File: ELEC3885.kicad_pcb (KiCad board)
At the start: 4 copper layers, 190 x 145.2 mm, 159 parts, among them J1 MicInstIn, J2 LineIn, J3 HeadPhoneOut, J4 Conn_01x05_Female, J5 LineOutR, J6 LineOutL, J7 USB_B_Micro, J8 Conn_LiPo, SW1 SW_SPST, SW10 RotaryEncoder_Switch, SW11 RotaryEncoder_Switch, SW12 RotaryEncoder_Switch, SW13 RotaryEncoder_Switch, SW14 SW_Push, SW15 SW_Push, SW16 SW_Push, SW17 SW_Push, SW2 SW_Push, SW3 SW_Push, SW4 SW_Push, SW5 SW_Push, SW6 SW_Push, SW7 SW_Push, SW8 SW_Push, SW9 SW_Push, U1 NE5532, U10 74HC595, U11 LCD_Conn, U2 AP7313, U3 SGTL5000XNLA3, U4 Teensy4.1, U5 MCP73831-2-OT, U6 MT3608, U7 L7805, U8 74HC595, U9 74HC595

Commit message: Rev4 started, changing packages
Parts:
- D2: footprint LED_SMD:LED_0603_1608Metric -> LED_SMD:LED_0201_0603Metric
- U10, U8, U9: footprint Package_SO:SOP-16_4.4x10.4mm_P1.27mm -> Package_SO:SOP-16_3.9x9.9mm_P1.27mm
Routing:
- net +5V: track 424.7 -> 418.9 mm, vias 19 -> 20
- net Net-(U10-QH'): track 50.6 -> 56.2 mm, vias 2 -> 4
- net /Teensy/LED_RCLK: track 158.0 -> 153.7 mm, vias 8 -> 6
- net /Teensy/LED_SRCLK: track 149.9 -> 153.8 mm
- net Net-(U10-QA): track 7.63 -> 11.0 mm
- net Net-(U10-~{OE}): track 105.0 -> 108.3 mm
- net /Teensy/LED_DS: track 53.4 -> 55.8 mm
- net Net-(U9-QA): track 24.3 -> 25.9 mm
- net Net-(U8-QH): track 23.9 -> 25.0 mm
- net Net-(U8-SER): track 71.9 -> 71.4 mm

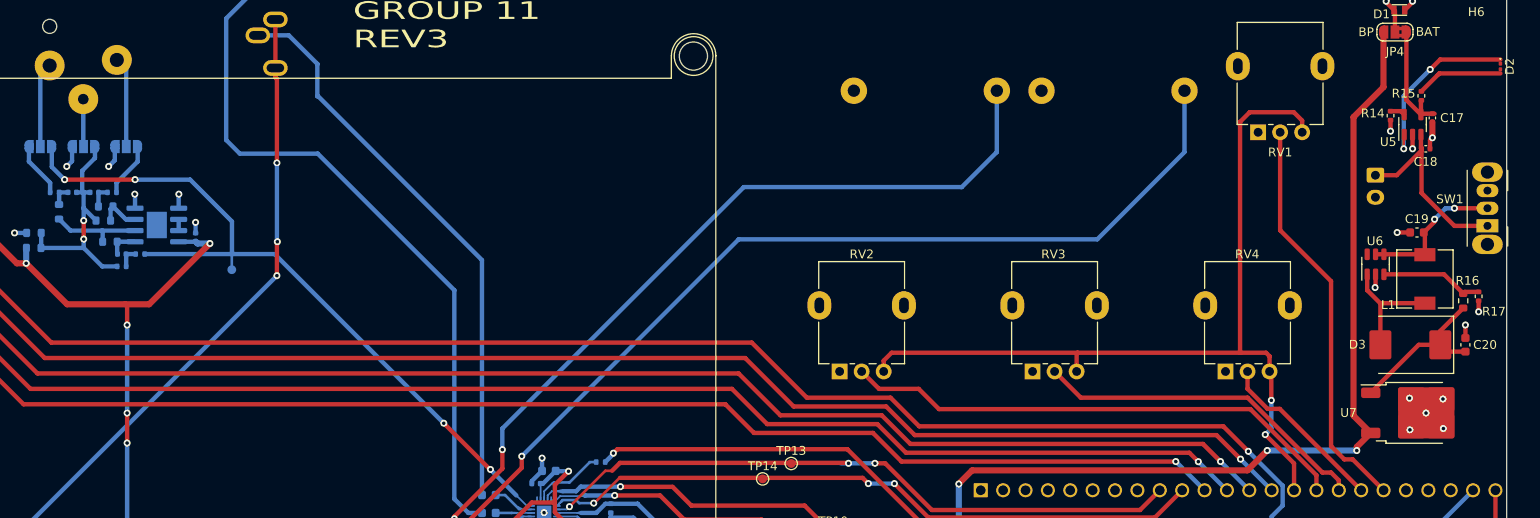
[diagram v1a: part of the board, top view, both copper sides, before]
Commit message: Footprints updated except codec
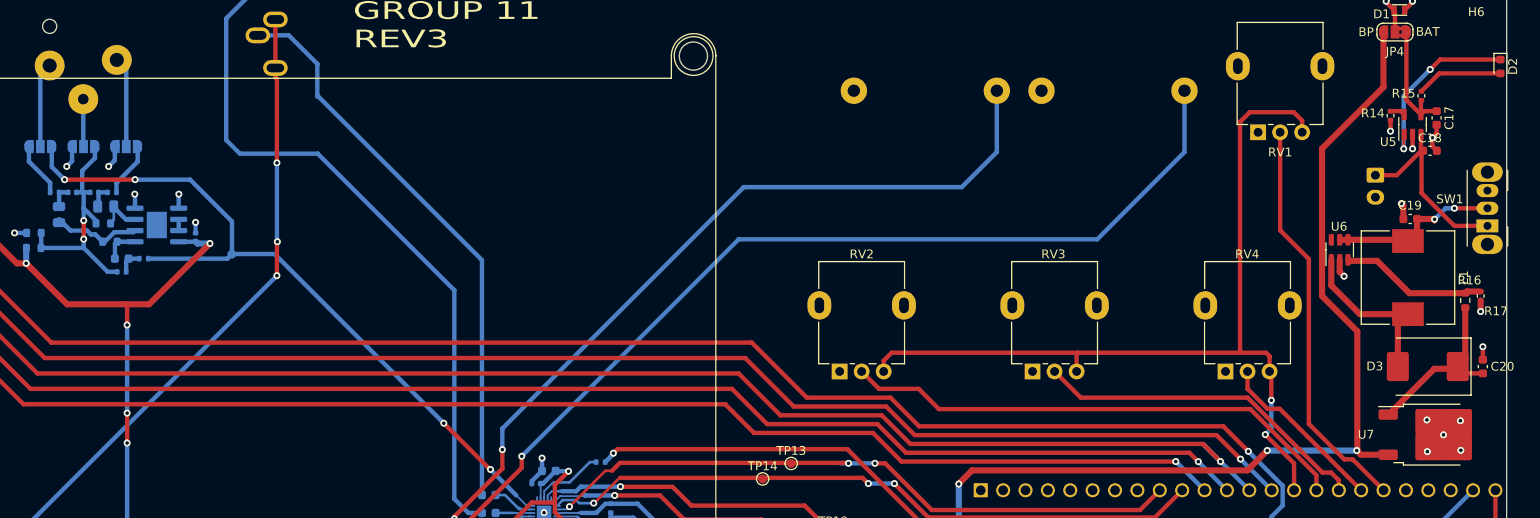
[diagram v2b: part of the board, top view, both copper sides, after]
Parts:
- C16, C17, C18: footprint Capacitor_SMD:C_0402_1005Metric -> Capacitor_SMD:C_0603_1608Metric
- D2: footprint LED_SMD:LED_0201_0603Metric -> LED_SMD:LED_0603_1608Metric
- L1: footprint Inductor_SMD:L_6.3x6.3_H3 -> Inductor_SMD:L_10.4x10.4_H4.8
- R8, R9: footprint Resistor_SMD:R_0603_1608Metric -> Resistor_SMD:R_0805_2012Metric
- moved U6 4.39 mm to (191.2, 51.5)
- moved C20 3.17 mm to (207.5, 64.8)
- moved D3 3.17 mm to (201.2, 64.8)
- moved U7 3.17 mm to (201.8, 72.5)
- moved L1 1.93 mm to (199.0, 54.6)
- moved TP7 1.75 mm to (65.5, 52.0)
- moved C19 1.71 mm to (199.2, 48.0)
- moved R13 0.66 mm to (55.5, 52.5)
- moved R12 0.62 mm to (53.0, 54.0)
- moved C18 0.53 mm to (201.5, 40.2)
- moved C16 0.52 mm to (53.0, 52.5)
- moved C17 0.48 mm to (202.2, 36.5)
- moved R10 0.32 mm to (50.9, 48.5)
- moved R8 0.32 mm to (45.9, 47.5)
- moved R16 0.23 mm to (205.5, 57.2)
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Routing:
- net Net-(D3-A): track 13.7 -> 19.4 mm
- net +5V: track 418.9 -> 424.4 mm
- net Net-(U6-FB): track 11.7 -> 16.7 mm
- net Net-(SW1-B): track 16.5 -> 19.5 mm
- net /Audio/MIC_IN: track 86.5 -> 84.6 mm
- net Net-(D3-K): track 17.5 -> 19.3 mm
- net GND: track 53.0 -> 54.2 mm
- net Net-(C16-Pad1): track 3.46 -> 4.05 mm

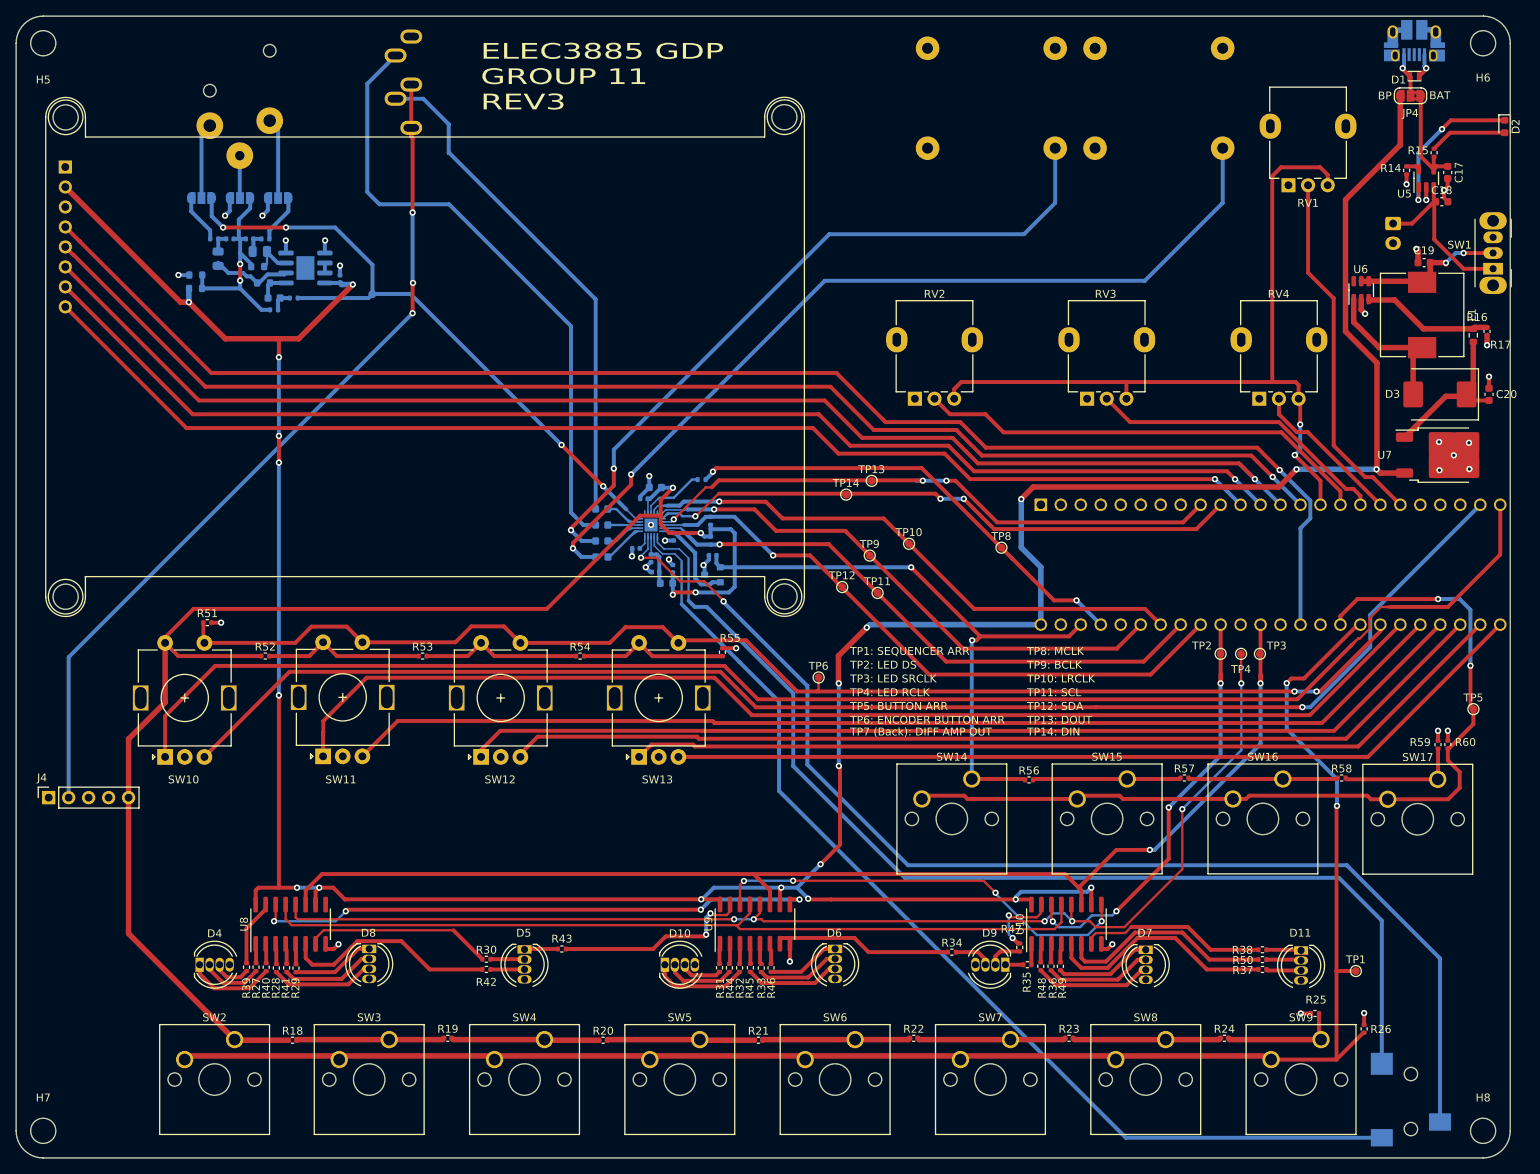
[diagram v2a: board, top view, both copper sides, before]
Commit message: SGTL5000 package switched to QFN32
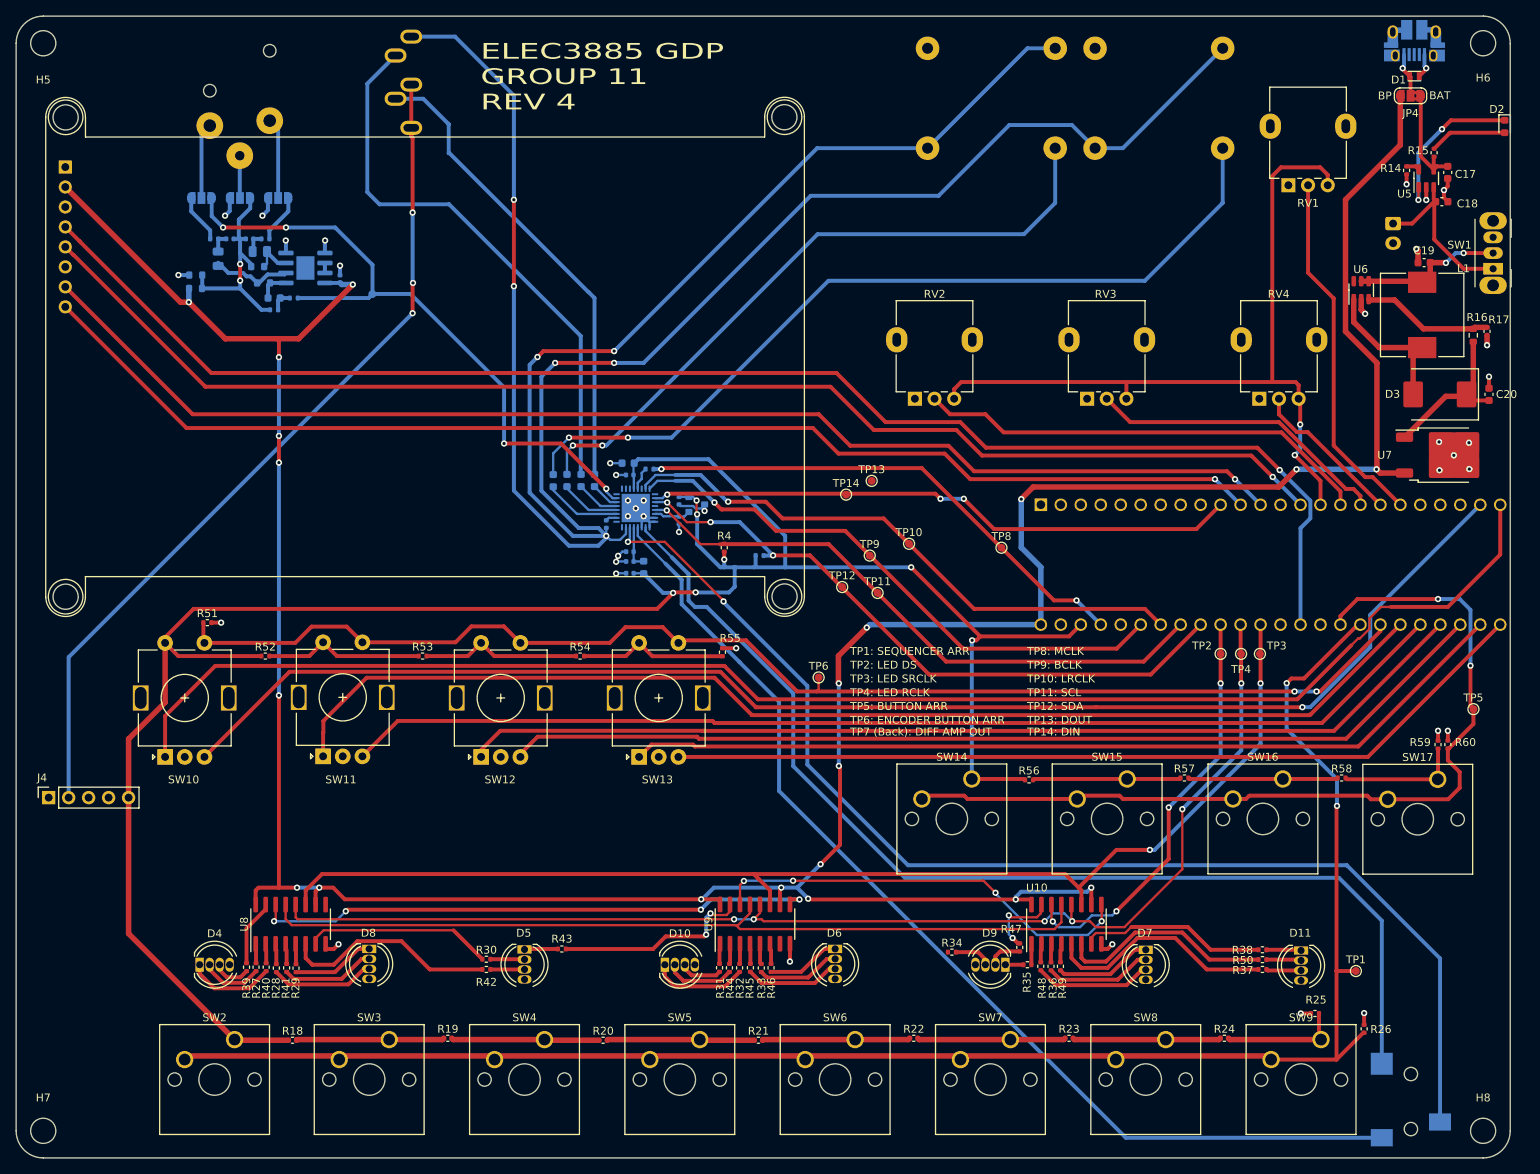
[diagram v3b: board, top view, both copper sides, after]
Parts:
- R4: moved to F.Cu
- U2: footprint LukeLibrary:SOT23 -> Luke_library:SOT23
- U3: value SGTL5000XNLA3 -> SGTL5000XNAA3; footprint Package_DFN_QFN:QFN-20-1EP_3x3mm_P0.4mm_EP1.65x1.65mm -> Package_DFN_QFN:QFN-32-1EP_5x5mm_P0.5mm_EP3.6x3.6mm
- moved C14 11.5 mm to (88.5, 75.7), turned to 90 degrees
- moved U2 9.16 mm to (106.8, 78.8), turned to 90 degrees
- moved C15 8.87 mm to (90.2, 75.7), turned to 90 degrees
- moved C4 8.17 mm to (104.5, 78.3), turned to -90 degrees
- moved R5 7.64 mm to (114.8, 85.2), turned to 180 degrees
- moved R3 6.76 mm to (100.8, 74.2)
- moved C5 6.24 mm to (92.0, 75.7), turned to -90 degrees
- moved C8 5.49 mm to (98.2, 87.5), turned to 180 degrees
- moved C7 4.89 mm to (95.2, 81.2), turned to 90 degrees
- moved C1 4.64 mm to (98.0, 73.5)
- moved C13 4.17 mm to (98.2, 84.8)
- moved C6 3.75 mm to (93.8, 75.7), turned to -90 degrees
- moved FB1 3.54 mm to (100.0, 86.8), turned to 90 degrees
- moved C3 3.53 mm to (98.2, 75.0)
- moved U3 2.91 mm to (99.0, 79.2)
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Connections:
- U3 pad 1: /Audio/HP_R -> GND
- U3 pad 10: /Audio/MIC_IN -> Net-(U3-VAG)
- U3 pad 11: /Audio/MIC_BIAS -> Net-(U3-LINEOUT_R)
- U3 pad 12: +3.3V -> Net-(U3-LINEOUT_L)
- U3 pad 13: Net-(U3-SYS_MCLK) -> Net-(U3-LINEIN_R)
- U3 pad 14: /Audio/LCLK -> Net-(U3-LINEIN_L)
- U3 pad 15: /Audio/BCLK -> /Audio/MIC_IN
- U3 pad 16: /Audio/D_IN -> unconnected-(U3-MIC_BIAS-Pad16)
- U3 pad 17: /Audio/D_OUT -> unconnected-(U3-NC-Pad17)
- U3 pad 18: /Audio/SDA -> unconnected-(U3-CPFILT-Pad18)
- U3 pad 19: /Audio/SCL -> unconnected-(U3-NC-Pad19)
- U3 pad 2: /Audio/HP_VGND -> /Audio/HP_R
- U3 pad 20: Net-(U2-Vout) -> +3.3V
- U3 pad 21: GND -> Net-(U3-SYS_MCLK)
- U3 pad 3: Net-(U3-VDDA) -> GND
- U3 pad 4: /Audio/HP_L -> /Audio/HP_VGND
- U3 pad 5: Net-(U3-VAG) -> Net-(U3-VDDA)
- U3 pad 6: Net-(U3-LINEOUT_R) -> /Audio/HP_L
- U3 pad 7: Net-(U3-LINEOUT_L) -> GND
- U3 pad 8: Net-(U3-LINEIN_R) -> unconnected-(U3-NC-Pad8)
- U3 pad 9: Net-(U3-LINEIN_L) -> unconnected-(U3-NC-Pad9)
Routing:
- net GND: track 54.2 -> 390.8 mm, vias 35 -> 47
- net /Teensy/LCD_MOSI: track 169.8 -> 0.00 mm, vias 1 -> 0
- net /Audio/D_OUT: track 74.3 -> 0.00 mm, vias 3 -> 0
- net Net-(U9-QH): track 23.4 -> 0.00 mm
- net +3.3V: track 365.2 -> 383.3 mm, vias 8 -> 9
- net /Audio/LINE_IN_R: track 79.3 -> 71.1 mm
- net Net-(U2-Vout): track 12.2 -> 4.63 mm
- net /Audio/LINE_OUT_L: track 92.3 -> 85.1 mm
- net /Audio/MCLK: track 59.1 -> 65.2 mm
- net Net-(U3-SYS_MCLK): track 8.11 -> 2.90 mm
- net Net-(U3-LINEOUT_R): track 5.18 -> 9.73 mm
- net /Audio/LINE_IN_L: track 64.9 -> 60.4 mm
- net /Audio/LINE_OUT_R: track 112.3 -> 108.0 mm
- net /Teensy/LED_RCLK: track 153.7 -> 156.9 mm
- net Net-(U3-LINEOUT_L): track 4.71 -> 7.44 mm
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- added copper zone on In1.Cu, net (none)
- added copper zone on In2.Cu, net (none)
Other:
- board text added: "ELEC3885 GDP GROUP 11 REV 4"
- board text removed: "ELEC3885 GDP GROUP 11 REV3"

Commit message: Fix unconnected tracks, add teardrops
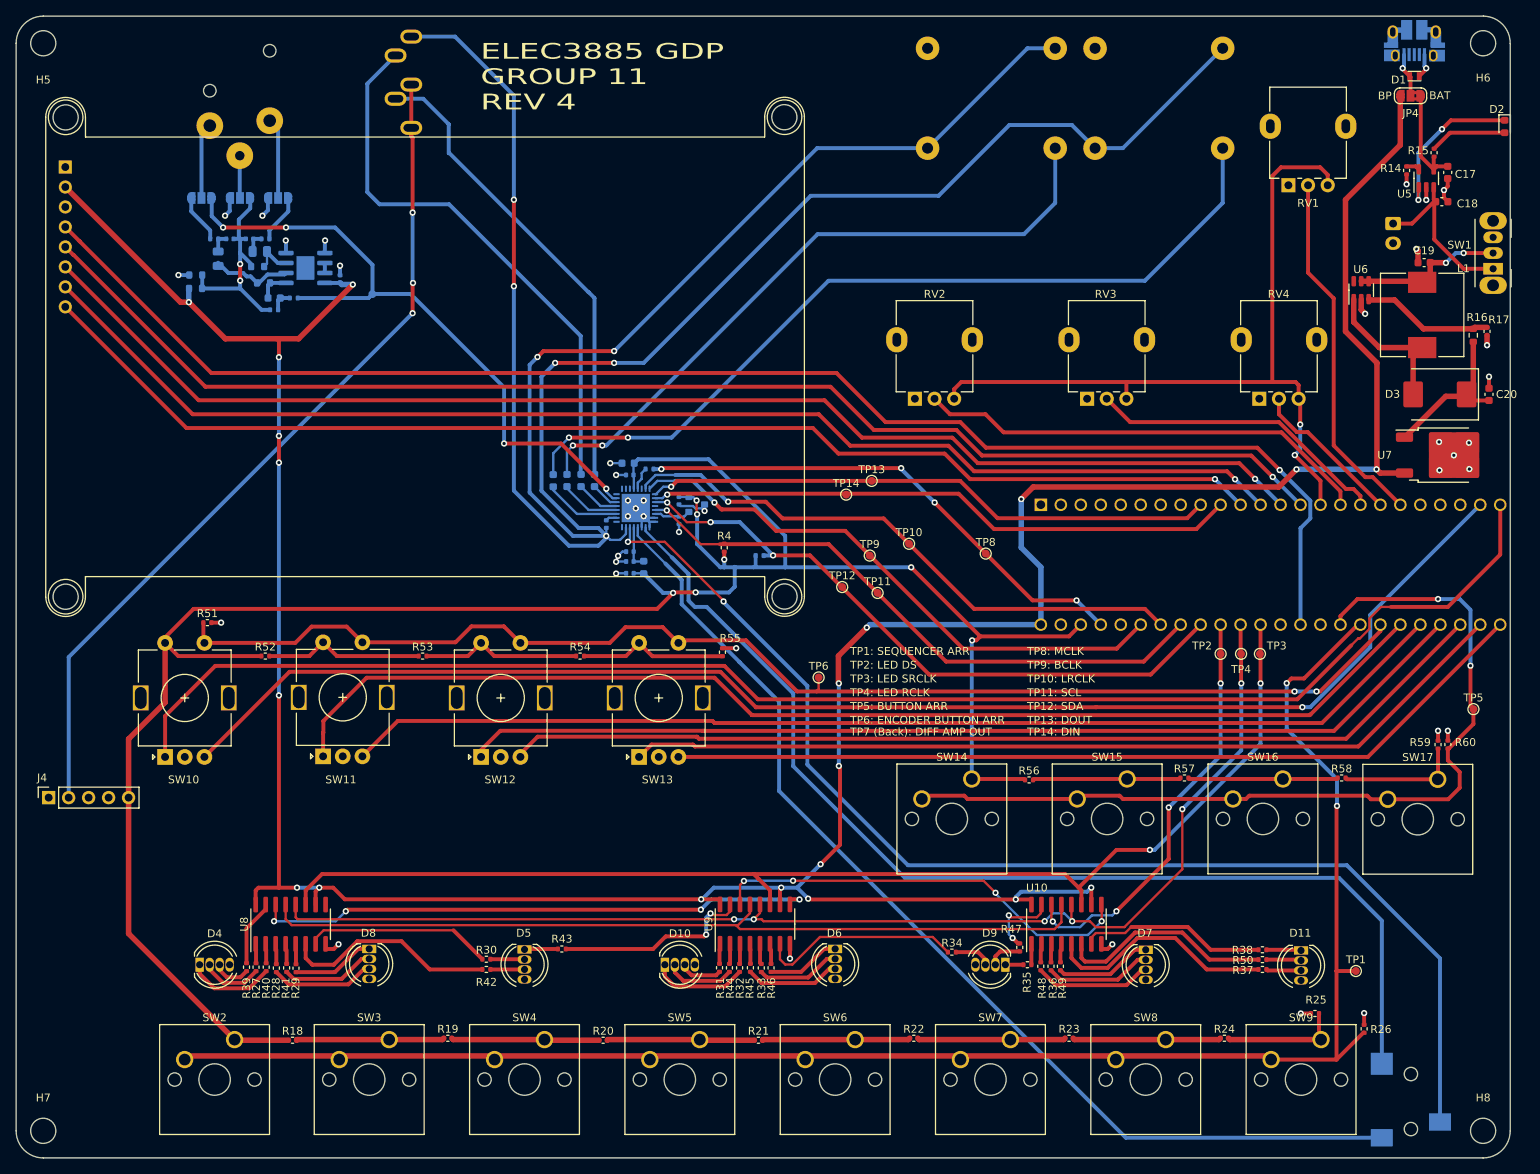
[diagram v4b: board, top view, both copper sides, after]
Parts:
- moved TP8 2.14 mm to (143.5, 85.0)
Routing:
- net /Teensy/LCD_MOSI: track 0.00 -> 167.0 mm, vias 0 -> 1
- net /Audio/D_OUT: track 0.00 -> 72.8 mm, vias 0 -> 1
- net Net-(U9-QH): track 0.00 -> 25.9 mm
- net /Audio/MCLK: vias 2 -> 4
- net /Audio/D_IN: vias 3 -> 1
